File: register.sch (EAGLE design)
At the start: 28 parts, among them IC1 74AS574N, IC2 74AS574N, IC3 74AC283N, IC4 74AC283N, IC5 74AC283N, IC6 74AC283N, IC7 74AC244N, IC8 74AC244N

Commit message: some work
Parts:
- added D1, D10, D11, D12, D13, D14, D15, D16, D2, D3, D4, D5, D6, D7, D8, D9: (no value), diode:DIODE-D-7.5
- added IC10: AND(08), 74xx-us:74ALS08N
- added IC9: NOT(04), 74xx-us:74ALS04N
- added JP5: (no value), pinhead:PINHD-1X7
- added JP6, JP7: (no value), pinhead:PINHD-1X8
- added JP8: (no value), pinhead:PINHD-1X2
- added R17, R18, R19, R20, R21, R22, R23: 10k, rcl:R-US_0204/7
- IC1, IC2: value 74AS574N -> D(574); MOUSER (none) -> 595-SN74HCT574NE4
- IC3, IC4, IC5, IC6: value 74AC283N -> ADD(283); MOUSER (none) -> 595-CD74HCT283E
- IC7, IC8: value 74AC244N -> BUF(244); MOUSER (none) -> 595-SN74HCT244NE4
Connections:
- removed net LSB: IC2A.8D, JP2.1
- removed net MSB: IC1A.1D, JP1.8
- removed net N$10: IC1A.7D, JP1.2
- removed net N$11: IC1A.6D, JP1.3
- removed net N$12: IC1A.5D, JP1.4
- removed net N$13: IC1A.4D, JP1.5
- removed net N$14: IC1A.3D, JP1.6
- removed net N$15: IC1A.2D, JP1.7
- removed net N$8: IC2A.1D, JP2.8
- removed net N$9: IC1A.8D, JP1.1
- new net 8BIT: IC1A.OC, JP5.2, R23.1
- new net B0: IC2A.8D, IC8B.Y1, JP2.1
- new net B1: IC2A.7D, IC8B.Y2, JP2.2
- new net B10: IC1A.6D, IC7B.Y3, JP1.3
- new net B11: IC1A.5D, IC7B.Y4, JP1.4
- new net B12: IC1A.4D, IC7A.Y1, JP1.5
- new net B13: IC1A.3D, IC7A.Y2, JP1.6
- new net B14: IC1A.2D, IC7A.Y3, JP1.7
- new net B15: IC1A.1D, IC7A.Y4, JP1.8
- new net B2: IC2A.6D, IC8B.Y3, JP2.3
- new net B3: IC2A.5D, IC8B.Y4, JP2.4
- new net B4: IC2A.4D, IC8A.Y1, JP2.5
- new net B5: IC2A.3D, IC8A.Y2, JP2.6
- new net B6: IC2A.2D, IC8A.Y3, JP2.7
- new net B7: IC2A.1D, IC8A.Y4, JP2.8
- new net B8: IC1A.8D, IC7B.Y1, JP1.1
- new net B9: IC1A.7D, IC7B.Y2, JP1.2
- new net CLK: IC10A.I0, JP5.7, R18.1
- new net CLK2: IC10B.O, IC1A.CLK, IC2A.CLK
- new net N$18: IC3A.S1, IC7A.A1
- new net N$19: IC3A.S2, IC7A.A2
- new net N$20: IC3A.S3, IC7A.A3
- new net N$21: IC3A.S4, IC7A.A4
- new net N$22: IC4A.S1, IC7B.A1
- new net N$23: IC4A.S2, IC7B.A2
- new net N$24: IC4A.S3, IC7B.A3
- new net N$25: IC4A.S4, IC7B.A4
- new net N$26: IC5A.S1, IC8A.A1
- new net N$27: IC5A.S2, IC8A.A2
- new net N$28: IC5A.S3, IC8A.A3
- new net N$29: IC5A.S4, IC8A.A4
- new net N$30: IC6A.S1, IC8B.A1
- new net N$47: IC6A.S2, IC8B.A2
- new net N$48: IC6A.S3, IC8B.A3
- new net N$49: IC6A.S4, IC8B.A4
- new net RD: IC9E.I, JP5.5, R20.1
- new net VCC: JP8.2
- new net WE: IC10A.I1, JP5.6, R19.1
- new net Z: IC9A.O, JP5.1
- net DEC: now also JP5.3, R22.1
- net GND: now also JP8.1, R17.1, R18.2, R19.2, R20.2, R21.2, R22.2, R23.2; no longer IC1A.OC
- net INC: now also JP5.4, R21.1
- net N$2: now also IC10A.O, IC10B.I0, IC9D.I; no longer IC2A.7D, JP2.2
- net N$3: now also D1.C, D10.C, D11.C, D12.C, D13.C, D14.C, D15.C, D16.C, D2.C, D3.C, D4.C, D5.C, D6.C, D7.C, D8.C, D9.C, IC9A.I, R17.2; no longer IC2A.6D, JP2.3
- net N$31: now also JP7.1
- net N$32: now also JP7.2
- net N$33: now also JP7.3
- net N$34: now also JP7.4
- net N$35: now also JP7.5
- net N$36: now also JP7.6
- net N$37: now also JP7.7
- net N$38: now also JP7.8
- net N$39: now also JP6.1
- net N$4: now also IC7A.G, IC7B.G, IC8A.G, IC8B.G, IC9E.O; no longer IC2A.5D, JP2.4
- net N$40: now also JP6.2
- net N$41: now also JP6.3
- net N$42: now also JP6.4
- net N$43: now also JP6.5
- net N$44: now also JP6.6
- net N$45: now also JP6.7
- net N$46: now also JP6.8
- net N$5: now also IC10B.I1, IC9B.O; no longer IC2A.4D, JP2.5
- net N$6: now also IC9B.I, IC9C.O; no longer IC2A.3D, JP2.6
- net N$7: now also IC9C.I, IC9D.O; no longer IC2A.2D, JP2.7
- net Q0: now also D16.A
- net Q1: now also D15.A
- net Q10: now also D6.A
- net Q11: now also D5.A
- net Q12: now also D4.A
- net Q13: now also D3.A
- net Q14: now also D2.A
- net Q15: now also D1.A
- net Q2: now also D14.A
- net Q3: now also D13.A
- net Q4: now also D12.A
- net Q5: now also D11.A
- net Q6: now also D10.A
- net Q7: now also D9.A
- net Q8: now also D8.A
- net Q9: now also D7.A
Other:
- moved on the sheet: IC7A, IC7B, IC8A, IC8B, JP3, JP4, R1, R10, R11, R12, R13, R14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

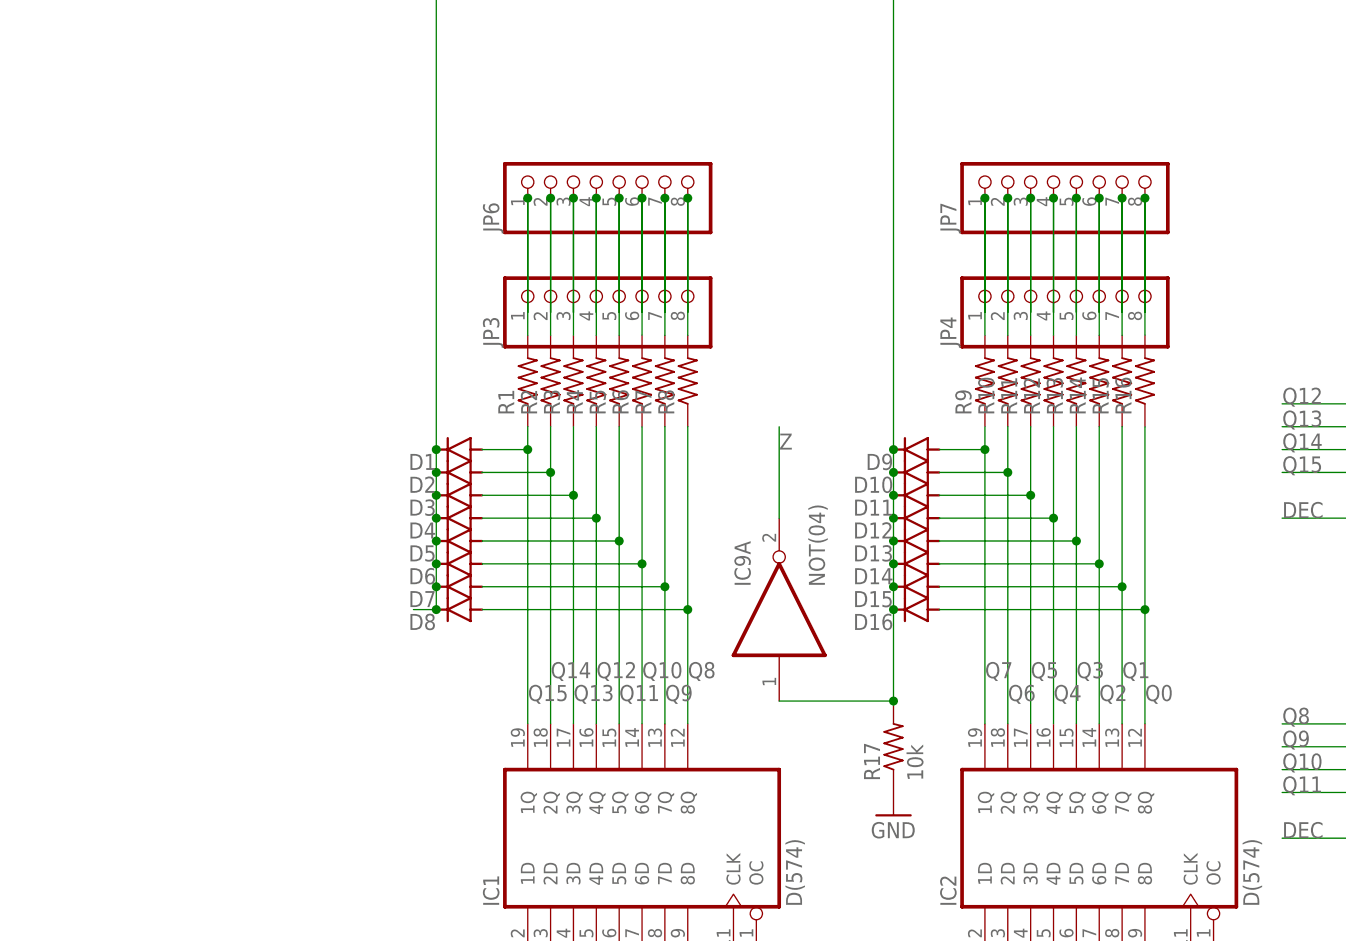
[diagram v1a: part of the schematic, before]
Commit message: mirror board, some docks
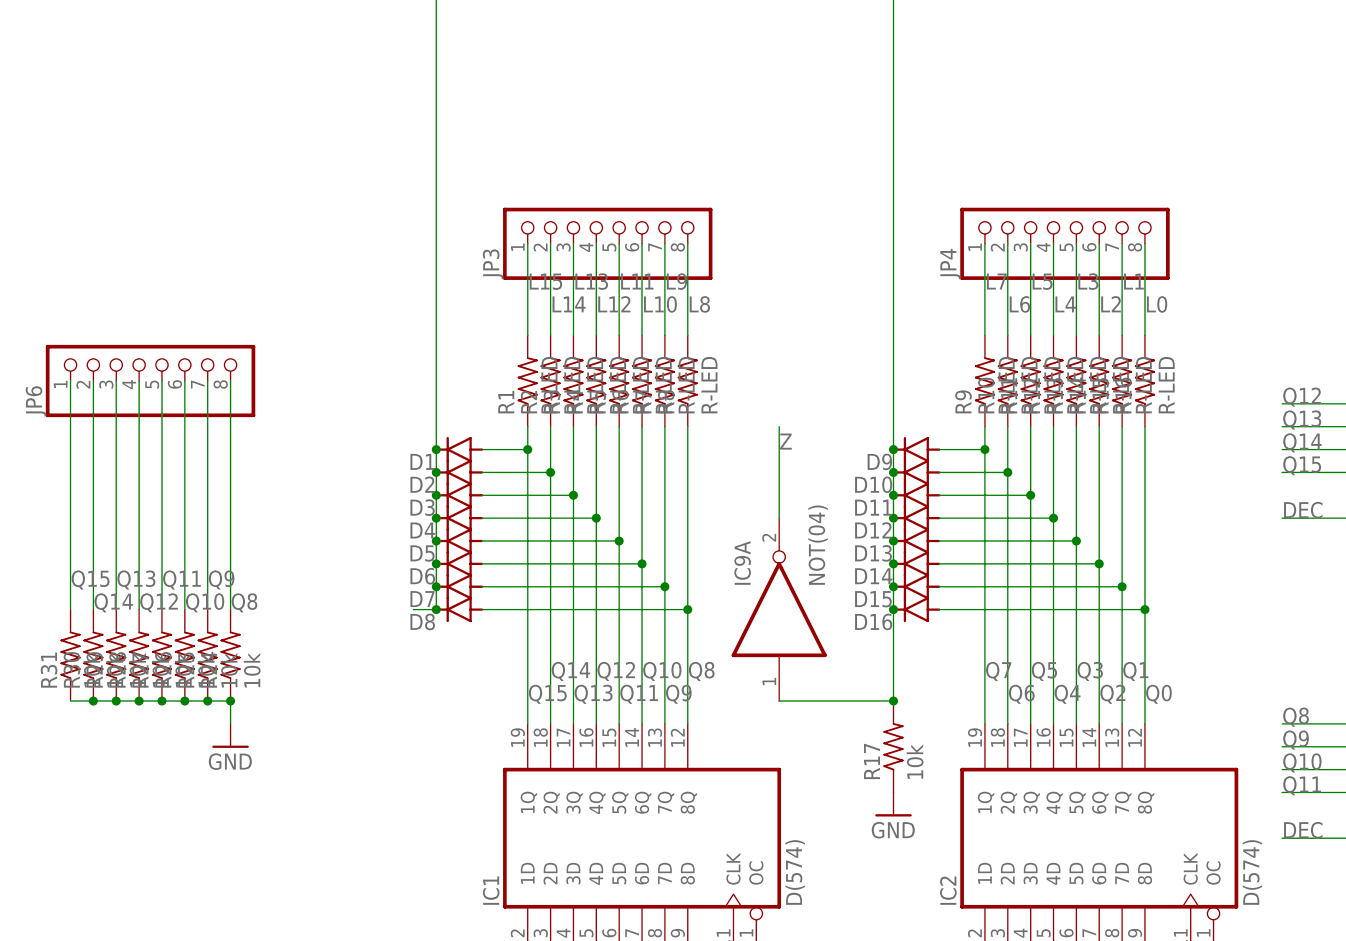
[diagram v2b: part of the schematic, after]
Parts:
- removed JP7: (no value), pinhead:PINHD-1X8
- added R24, R25, R26, R27, R28, R29, R30, R31: 10k, rcl:R-US_0204/7
- R1, R10, R11, R12, R13, R14, R15, R16, R2, R3, R4, R5, R6, R7, R8, R9: value (none) -> R-LED
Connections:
- removed net N$31: JP4.1, JP7.1, R9.2
- removed net N$32: JP4.2, JP7.2, R10.2
- removed net N$33: JP4.3, JP7.3, R11.2
- removed net N$34: JP4.4, JP7.4, R12.2
- removed net N$35: JP4.5, JP7.5, R13.2
- removed net N$36: JP4.6, JP7.6, R14.2
- removed net N$37: JP4.7, JP7.7, R15.2
- removed net N$38: JP4.8, JP7.8, R16.2
- removed net N$39: JP3.1, JP6.1, R1.2
- removed net N$40: JP3.2, JP6.2, R2.2
- removed net N$41: JP3.3, JP6.3, R3.2
- removed net N$42: JP3.4, JP6.4, R4.2
- removed net N$43: JP3.5, JP6.5, R5.2
- removed net N$44: JP3.6, JP6.6, R6.2
- removed net N$45: JP3.7, JP6.7, R7.2
- removed net N$46: JP3.8, JP6.8, R8.2
- new net L0: JP4.8, R16.2
- new net L1: JP4.7, R15.2
- new net L10: JP3.6, R6.2
- new net L11: JP3.5, R5.2
- new net L12: JP3.4, R4.2
- new net L13: JP3.3, R3.2
- new net L14: JP3.2, R2.2
- new net L15: JP3.1, R1.2
- new net L2: JP4.6, R14.2
- new net L3: JP4.5, R13.2
- new net L4: JP4.4, R12.2
- new net L5: JP4.3, R11.2
- new net L6: JP4.2, R10.2
- new net L7: JP4.1, R9.2
- new net L8: JP3.8, R8.2
- new net L9: JP3.7, R7.2
- net GND: now also R24.1, R25.1, R26.1, R27.1, R28.1, R29.1, R30.1, R31.1
- net Q10: now also JP6.6, R26.2
- net Q11: now also JP6.5, R27.2
- net Q12: now also JP6.4, R28.2
- net Q13: now also JP6.3, R29.2
- net Q14: now also JP6.2, R30.2
- net Q15: now also JP6.1, R31.2
- net Q8: now also JP6.8, R24.2
- net Q9: now also JP6.7, R25.2
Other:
- moved on the sheet: JP3, JP4, JP6

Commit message: add gerbers
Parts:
- added C1, C2, C3, C4, C5: C-Decouple, rcl:C-EU025-025X050
- added H1, H2, H3: MOUNT-HOLE3.0, holes:MOUNT-HOLE3.0
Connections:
- net GND: now also C1.2, C2.2, C3.2, C4.2, C5.2
- net VCC: now also C1.1, C2.1, C3.1, C4.1, C5.1
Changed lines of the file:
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@@
 </part>
 <part name="GND5" library="supply1" library_urn="urn:adsk.eagle:library:371" deviceset="GND" device=""/>
+<part name="C1" library="rcl" library_urn="urn:adsk.eagle:library:334" deviceset="C-EU" device="025-025X050" package3d_urn="urn:adsk.eagle:package:23629/2" value="C-Decouple"/>
+<part name="C2" library="rcl" library_urn="urn:adsk.eagle:library:334" deviceset="C-EU" device="025-025X050" package3d_urn="urn:adsk.eagle:package:23629/2" value="C-Decouple"/>
+<part name="C3" library="rcl" library_urn="urn:adsk.eagle:library:334" deviceset="C-EU" device="025-025X050" package3d_urn="urn:adsk.eagle:package:23629/2" value="C-Decouple"/>
+<part name="C4" library="rcl" library_urn="urn:adsk.eagle:library:334" deviceset="C-EU" device="025-025X050" package3d_urn="urn:adsk.eagle:package:23629/2" value="C-Decouple"/>
+<part name="C5" library="rcl" library_urn="urn:adsk.eagle:library:334" deviceset="C-EU" device="025-025X050" package3d_urn="urn:adsk.eagle:package:23629/2" value="C-Decouple"/>
+<part name="P+2" library="supply1" library_urn="urn:adsk.eagle:library:371" deviceset="VCC" device=""/>
+<part name="P+3" library="supply1" library_urn="urn:adsk.eagle:library:371" deviceset="VCC" device=""/>
+<part name="P+4" library="supply1" library_urn="urn:adsk.eagle:library:371" deviceset="VCC" device=""/>
+<part name="P+5" library="supply1" library_urn="urn:adsk.eagle:library:371" deviceset="VCC" device=""/>
+<part name="P+6" library="supply1" library_urn="urn:adsk.eagle:library:371" deviceset="VCC" device=""/>
+<part name="GND6" library="supply1" library_urn="urn:adsk.eagle:library:371" deviceset="GND" device=""/>
+<part name="GND7" library="supply1" library_urn="urn:adsk.eagle:library:371" deviceset="GND" device=""/>
+<part name="GND8" library="supply1" library_urn="urn:adsk.eagle:library:371" deviceset="GND" device=""/>
+<part name="GND9" library="supply1" library_urn="urn:adsk.eagle:library:371" deviceset="GND" device=""/>
+<part name="GND10" library="supply1" library_urn="urn:adsk.eagle:library:371" deviceset="GND" device=""/>
+<part name="H1" library="holes" library_urn="urn:adsk.eagle:library:237" deviceset="MOUNT-HOLE" device="3.0" package3d_urn="urn:adsk.eagle:package:14277/1"/>
+<part name="H2" library="holes" library_urn="urn:adsk.eagle:library:237" deviceset="MOUNT-HOLE" device="3.0" package3d_urn="urn:adsk.eagle:package:14277/1"/>
+<part name="H3" library="holes" library_urn="urn:adsk.eagle:library:237" deviceset="MOUNT-HOLE" device="3.0" package3d_urn="urn:adsk.eagle:package:14277/1"/>
 </parts>
 <sheets>
@@
 <instance part="GND5" gate="1" x="-7.62" y="71.12" smashed="yes">
 <attribute name="VALUE" x="-10.16" y="68.58" size="1.778" layer="96"/>
+</instance>
+<instance part="C1" gate="G$1" x="48.26" y="-45.72" smashed="yes">
+<attribute name="NAME" x="49.784" y="-45.339" size="1.778" layer="95"/>
+</instance>
+<instance part="C2" gate="G$1" x="53.34" y="-45.72" smashed="yes">
+<attribute name="NAME" x="54.864" y="-45.339" size="1.778" layer="95"/>
+</instance>
+<instance part="C3" gate="G$1" x="58.42" y="-45.72" smashed="yes">
+<attribute name="NAME" x="59.944" y="-45.339" size="1.778" layer="95"/>
+</instance>
+<instance part="C4" gate="G$1" x="63.5" y="-45.72" smashed="yes">
+<attribute name="NAME" x="65.024" y="-45.339" size="1.778" layer="95"/>
+</instance>
+<instance part="C5" gate="G$1" x="68.58" y="-45.72" smashed="yes">
+<attribute name="NAME" x="70.104" y="-45.339" size="1.778" layer="95"/>
+</instance>
+<instance part="P+2" gate="VCC" x="48.26" y="-40.64" smashed="yes">
+<attribute name="VALUE" x="45.72" y="-43.18" size="1.778" layer="96" rot="R90"/>
+</instance>
+<instance part="P+3" gate="VCC" x="53.34" y="-40.64" smashed="yes">
+<attribute name="VALUE" x="50.8" y="-43.18" size="1.778" layer="96" rot="R90"/>
+</instance>
+<instance part="P+4" gate="VCC" x="58.42" y="-40.64" smashed="yes">
+<attribute name="VALUE" x="55.88" y="-43.18" size="1.778" layer="96" rot="R90"/>
+</instance>
+<instance part="P+5" gate="VCC" x="63.5" y="-40.64" smashed="yes">
+<attribute name="VALUE" x="60.96" y="-43.18" size="1.778" layer="96" rot="R90"/>
+</instance>
+<instance part="P+6" gate="VCC" x="68.58" y="-40.64" smashed="yes">
+<attribute name="VALUE" x="66.04" y="-43.18" size="1.778" layer="96" rot="R90"/>
+</instance>
+<instance part="GND6" gate="1" x="48.26" y="-53.34" smashed="yes">
+<attribute name="VALUE" x="45.72" y="-55.88" size="1.778" layer="96"/>
+</instance>
+<instance part="GND7" gate="1" x="53.34" y="-53.34" smashed="yes">
+<attribute name="VALUE" x="50.8" y="-55.88" size="1.778" layer="96"/>
+</instance>
+<instance part="GND8" gate="1" x="58.42" y="-53.34" smashed="yes">
+<attribute name="VALUE" x="55.88" y="-55.88" size="1.778" layer="96"/>
+</instance>
+<instance part="GND9" gate="1" x="63.5" y="-53.34" smashed="yes">
+<attribute name="VALUE" x="60.96" y="-55.88" size="1.778" layer="96"/>
+</instance>
+<instance part="GND10" gate="1" x="68.58" y="-53.34" smashed="yes">
+<attribute name="VALUE" x="66.04" y="-55.88" size="1.778" layer="96"/>
+</instance>
+<instance part="H1" gate="G$1" x="-22.86" y="-22.86" smashed="yes">
+<attribute name="NAME" x="-20.828" y="-22.2758" size="1.778" layer="95"/>
+<attribute name="VALUE" x="-20.828" y="-25.3238" size="1.778" layer="96"/>
+</instance>
+<instance part="H2" gate="G$1" x="-22.86" y="-10.16" smashed="yes">
+<attribute name="NAME" x="-20.828" y="-9.5758" size="1.778" layer="95"/>
+<attribute name="VALUE" x="-20.828" y="-12.6238" size="1.778" layer="96"/>
+</instance>
+<instance part="H3" gate="G$1" x="7.62" y="-12.7" smashed="yes">
+<attribute name="NAME" x="9.652" y="-12.1158" size="1.778" layer="95"/>
+<attribute name="VALUE" x="9.652" y="-15.1638" size="1.778" layer="96"/>
 </instance>
 </instances>
@@
 <junction x="-15.24" y="76.2"/>
 <junction x="-12.7" y="76.2"/>
+</segment>
+<segment>
+<pinref part="C1" gate="G$1" pin="2"/>
+<pinref part="GND6" gate="1" pin="GND"/>
+</segment>
+<segment>
+<pinref part="C2" gate="G$1" pin="2"/>
+<pinref part="GND7" gate="1" pin="GND"/>
+</segment>
+<segment>
+<pinref part="C3" gate="G$1" pin="2"/>
+<pinref part="GND8" gate="1" pin="GND"/>
+</segment>
+<segment>
+<pinref part="C4" gate="G$1" pin="2"/>
+<pinref part="GND9" gate="1" pin="GND"/>
+</segment>
+<segment>
+<pinref part="C5" gate="G$1" pin="2"/>
+<pinref part="GND10" gate="1" pin="GND"/>
 </segment>
 </net>
@@
 <wire x1="91.44" y1="-7.62" x2="91.44" y2="-17.78" width="0.1524" layer="91"/>
 </segment>
-</net>
+<segment>
+<pinref part="C1" gate="G$1" pin="1"/>
+<pinref part="P+2" gate="VCC" pin="VCC"/>
+</segment>
+<segment>
+<pinref part="C2" gate="G$1" pin="1"/>
+<pinref part="P+3" gate="VCC" pin="VCC"/>
+</segment>
+<segment>
+<pinref part="C3" gate="G$1" pin="1"/>
+<pinref part="P+4" gate="VCC" pin="VCC"/>
+</segment>
+<segment>
+<pinref part="C4" gate="G$1" pin="1"/>
+<pinref part="P+5" gate="VCC" pin="VCC"/>
+</segment>
+<segment>
+<pinref part="C5" gate="G$1" pin="1"/>
+<pinref part="P+6" gate="VCC" pin="VCC"/>
+</segment>
+</net>
